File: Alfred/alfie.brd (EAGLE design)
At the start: 83.9 x 45 mm, 33 parts, among them IC1 7805TV, K1 G6A-234P, K2 G6A-234P

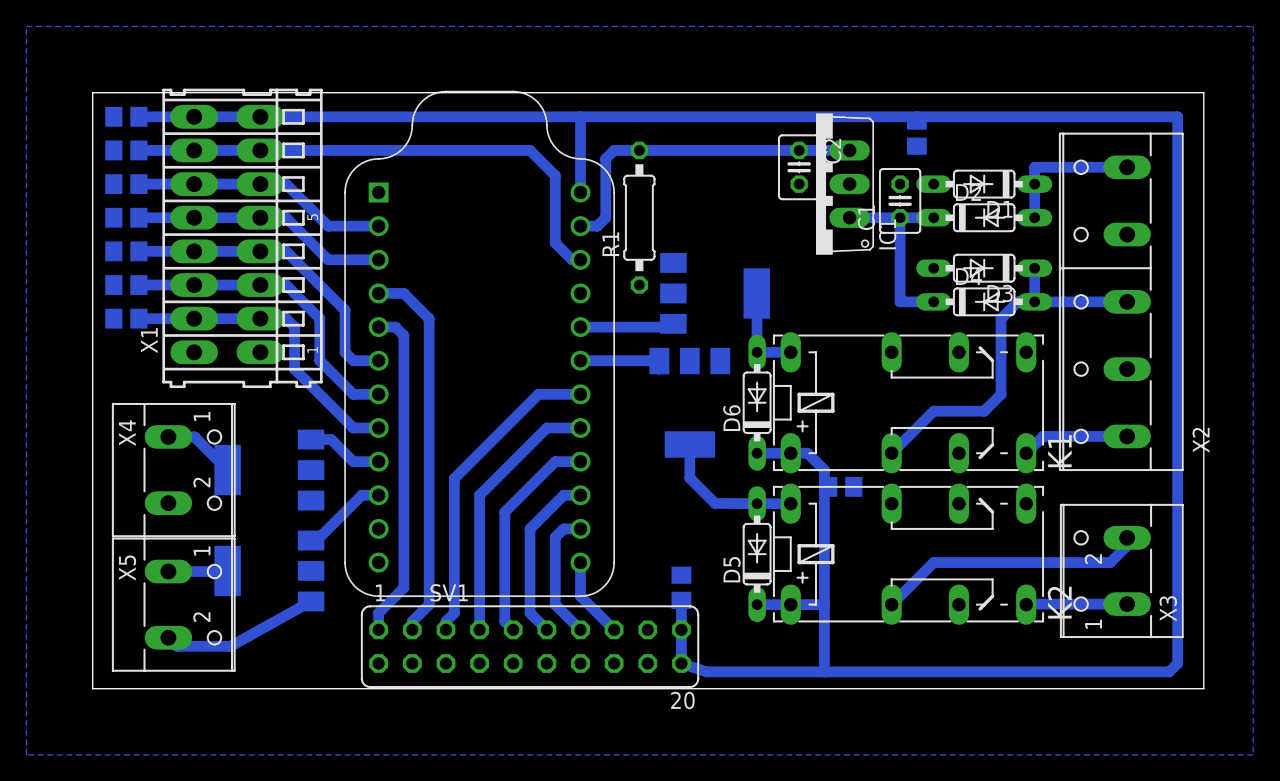
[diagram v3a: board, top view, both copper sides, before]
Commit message: Added bigass cap for relays
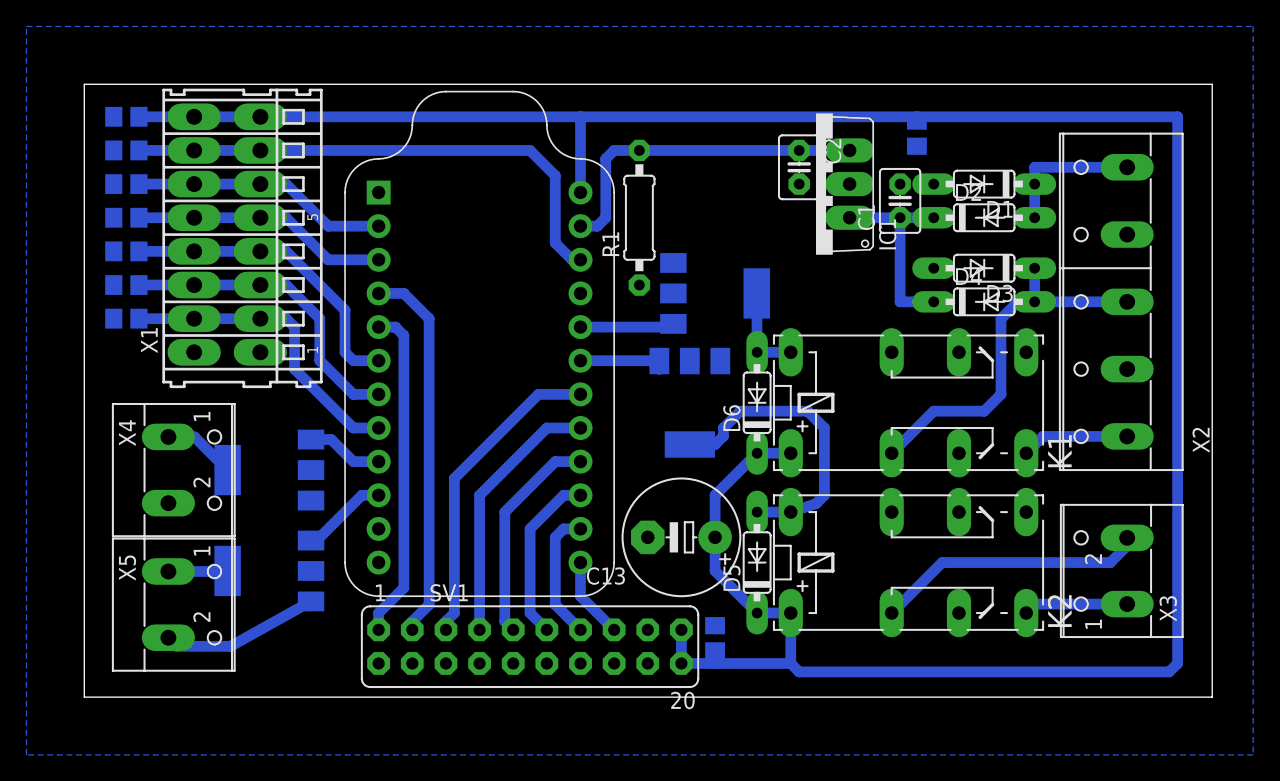
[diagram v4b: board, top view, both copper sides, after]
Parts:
- removed C12: 100nF, rcl:C0805
- added C13: (no value), rcl:E5-8,5
- moved C11 4.58 mm to (47.0, 3.81)
- moved D5 0.63 mm to (50.2, 9.53)
- moved K2 0.63 mm to (56.5, 9.53)
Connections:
- net +5V: now also C13.+; no longer C12.1
- net GND: now also C13.-; no longer C12.2
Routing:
- net N$2: track 10.9 -> 22.6 mm
- net +5V: track 194.6 -> 190.8 mm
- net N$4: track 7.64 -> 8.26 mm
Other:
- board size 83.9 x 45 mm -> 85.2 x 46.3 mm
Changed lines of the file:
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@@
 <board>
 <plain>
-<wire x1="0" y1="0" x2="83.89" y2="0" width="0" layer="20"/>
-<wire x1="83.89" y1="0" x2="83.89" y2="45" width="0" layer="20"/>
-<wire x1="83.89" y1="45" x2="0" y2="45" width="0" layer="20"/>
-<wire x1="0" y1="45" x2="0" y2="0" width="0" layer="20"/>
+<wire x1="-0.635" y1="-0.635" x2="84.525" y2="-0.635" width="0" layer="20"/>
+<wire x1="84.525" y1="-0.635" x2="84.525" y2="45.635" width="0" layer="20"/>
+<wire x1="84.525" y1="45.635" x2="-0.635" y2="45.635" width="0" layer="20"/>
+<wire x1="-0.635" y1="45.635" x2="-0.635" y2="-0.635" width="0" layer="20"/>
 </plain>
 <attributes>
@@
 <param name="rvMicroViaOuter" value="0.25"/>
 <param name="rvMicroViaInner" value="0.25"/>
-<param name="rlMinPadTop" value="10mil"/>
+<param name="rlMinPadTop" value="16mil"/>
 <param name="rlMaxPadTop" value="20mil"/>
-<param name="rlMinPadInner" value="10mil"/>
+<param name="rlMinPadInner" value="16mil"/>
 <param name="rlMaxPadInner" value="20mil"/>
-<param name="rlMinPadBottom" value="10mil"/>
+<param name="rlMinPadBottom" value="16mil"/>
 <param name="rlMaxPadBottom" value="20mil"/>
 <param name="rlMinViaOuter" value="8mil"/>
@@
 <param name="rlMinMicroViaInner" value="4mil"/>
 <param name="rlMaxMicroViaInner" value="20mil"/>
-<param name="psTop" value="-1"/>
-<param name="psBottom" value="-1"/>
+<param name="psTop" value="2"/>
+<param name="psBottom" value="2"/>
 <param name="psFirst" value="-1"/>
 <param name="psElongationLong" value="100"/>
@@
 <param name="checkFont" value="1"/>
 <param name="checkRestrict" value="1"/>
-<param name="useDiameter" value="13"/>
+<param name="useDiameter" value="15"/>
 <param name="maxErrors" value="999999"/>
 </designrules>
@@
 </element>
 <element name="U$5" library="NTF3055L108" package="SOT223" value="NTF3055L108T1GTAB" x="45.085" y="21.59" rot="MR180"/>
-<element name="K2" library="relay" package="G6A-234P" value="G6A-234P" x="56.515" y="10.16">
-<attribute name="OC_NEWARK" value="unknown" x="47.625" y="10.16" size="1.778" layer="27" display="off"/>
-<attribute name="MPN" value="" x="47.625" y="10.16" size="1.778" layer="27" display="off"/>
-<attribute name="MF" value="" x="47.625" y="10.16" size="1.778" layer="27" display="off"/>
-<attribute name="OC_FARNELL" value="unknown" x="47.625" y="10.16" size="1.778" layer="27" display="off"/>
+<element name="K2" library="relay" package="G6A-234P" value="G6A-234P" x="56.515" y="9.525">
+<attribute name="OC_NEWARK" value="unknown" x="47.625" y="9.525" size="1.778" layer="27" display="off"/>
+<attribute name="MPN" value="" x="47.625" y="9.525" size="1.778" layer="27" display="off"/>
+<attribute name="MF" value="" x="47.625" y="9.525" size="1.778" layer="27" display="off"/>
+<attribute name="OC_FARNELL" value="unknown" x="47.625" y="9.525" size="1.778" layer="27" display="off"/>
 </element>
 <element name="X3" library="con-wago-500" package="W237-102" value="" x="76.835" y="8.89" rot="R90">
@@
 <attribute name="OC_FARNELL" value="unknown" x="76.835" y="8.89" size="1.778" layer="27" rot="R90" display="off"/>
 </element>
-<element name="D5" library="diode" package="DO35-7" value="1N4148DO35-7" x="50.165" y="10.16" rot="R90"/>
+<element name="D5" library="diode" package="DO35-7" value="1N4148DO35-7" x="50.165" y="9.525" rot="R90"/>
 <element name="D6" library="diode" package="DO35-7" value="1N4148DO35-7" x="50.165" y="21.59" rot="R90"/>
 <element name="R1" library="rcl" package="0207/10" value="" x="41.275" y="35.56" rot="R90"/>
@@
 <element name="C9" library="rcl" package="C0805" value="100nF" x="2.54" y="43.18" rot="MR0"/>
 <element name="C10" library="rcl" package="C0805" value="100nF" x="62.23" y="41.91" rot="MR270"/>
-<element name="C11" library="rcl" package="C0805" value="100nF" x="44.45" y="7.62" rot="MR90"/>
-<element name="C12" library="rcl" package="C0805" value="100nF" x="56.515" y="15.24" rot="MR180"/>
+<element name="C11" library="rcl" package="C0805" value="100nF" x="46.99" y="3.81" rot="MR90"/>
+<element name="C13" library="rcl" package="E5-8,5" value="" x="44.45" y="11.43" rot="R180"/>
 </elements>
 <signals>
@@
 <wire x1="36.83" y1="37.465" x2="36.83" y2="43.18" width="0.8128" layer="16"/>
 <wire x1="81.915" y1="1.905" x2="81.28" y2="1.27" width="0.8128" layer="16"/>
-<wire x1="81.28" y1="1.27" x2="55.245" y2="1.27" width="0.8128" layer="16"/>
+<wire x1="81.28" y1="1.27" x2="53.34" y2="1.27" width="0.8128" layer="16"/>
 <contactref element="K2" pad="1"/>
-<wire x1="55.245" y1="1.27" x2="46.355" y2="1.27" width="0.8128" layer="16"/>
-<wire x1="55.245" y1="1.27" x2="55.245" y2="6.35" width="0.8128" layer="16"/>
-<wire x1="55.245" y1="6.35" x2="55.245" y2="15.24" width="0.8128" layer="16"/>
-<wire x1="55.245" y1="15.24" x2="55.245" y2="16.51" width="0.8128" layer="16"/>
-<wire x1="55.245" y1="16.51" x2="53.975" y2="17.78" width="0.8128" layer="16"/>
-<wire x1="53.975" y1="17.78" x2="52.705" y2="17.78" width="0.8128" layer="16"/>
-<wire x1="52.705" y1="6.35" x2="55.245" y2="6.35" width="0.8128" layer="16"/>
 <contactref element="D5" pad="C"/>
 <contactref element="D6" pad="C"/>
-<wire x1="50.165" y1="6.35" x2="52.705" y2="6.35" width="0.8128" layer="16"/>
-<wire x1="50.165" y1="17.78" x2="52.705" y2="17.78" width="0.8128" layer="16"/>
 <contactref element="SV1" pad="19"/>
 <contactref element="SV1" pad="20"/>
 <wire x1="44.45" y1="4.445" x2="44.45" y2="1.905" width="0.8128" layer="16"/>
-<wire x1="44.45" y1="1.905" x2="46.355" y2="1.27" width="0.8128" layer="16"/>
 <wire x1="12.66" y1="43.18" x2="36.83" y2="43.18" width="0.8128" layer="16"/>
 <contactref element="C9" pad="1"/>
 <wire x1="12.66" y1="43.18" x2="3.49" y2="43.18" width="0.8128" layer="16"/>
-<contactref element="C12" pad="1"/>
 <contactref element="C11" pad="1"/>
 <contactref element="C10" pad="1"/>
-<wire x1="44.45" y1="6.67" x2="44.45" y2="4.445" width="0.8128" layer="16"/>
-<wire x1="55.565" y1="15.24" x2="55.245" y2="15.24" width="0.8128" layer="16"/>
 <wire x1="62.23" y1="42.86" x2="62.23" y2="43.18" width="0.8128" layer="16"/>
+<contactref element="C13" pad="+"/>
+<wire x1="52.705" y1="17.78" x2="50.165" y2="17.78" width="0.8128" layer="16"/>
+<wire x1="53.34" y1="1.27" x2="52.705" y2="1.905" width="0.8128" layer="16"/>
+<wire x1="52.705" y1="1.905" x2="52.705" y2="5.715" width="0.8128" layer="16"/>
+<wire x1="52.705" y1="5.715" x2="50.165" y2="5.715" width="0.8128" layer="16"/>
+<wire x1="50.165" y1="5.715" x2="46.99" y2="8.89" width="0.8128" layer="16"/>
+<wire x1="46.99" y1="8.89" x2="46.99" y2="11.43" width="0.8128" layer="16"/>
+<wire x1="44.45" y1="1.905" x2="46.99" y2="1.905" width="0.8128" layer="16"/>
+<wire x1="46.99" y1="1.905" x2="52.705" y2="1.905" width="0.8128" layer="16"/>
+<wire x1="46.99" y1="2.86" x2="46.99" y2="1.905" width="0.8128" layer="16"/>
+<wire x1="50.165" y1="17.78" x2="46.99" y2="14.605" width="0.8128" layer="16"/>
+<wire x1="46.99" y1="14.605" x2="46.99" y2="11.43" width="0.8128" layer="16"/>
 </signal>
 <signal name="GND">
@@
 <contactref element="C10" pad="2"/>
 <contactref element="C11" pad="2"/>
-<contactref element="C12" pad="2"/>
+<contactref element="C13" pad="-"/>
 </signal>
 <signal name="DATA0">
@@
 <contactref element="U$5" pad="4"/>
 <contactref element="D5" pad="A"/>
-<wire x1="50.165" y1="13.97" x2="52.705" y2="13.97" width="0.8128" layer="16"/>
-<wire x1="50.165" y1="13.97" x2="46.99" y2="13.995" width="0.8128" layer="16"/>
-<wire x1="46.99" y1="13.995" x2="45.085" y2="15.9" width="0.8128" layer="16"/>
-<wire x1="45.085" y1="15.9" x2="45.085" y2="18.44" width="0.8128" layer="16"/>
+<wire x1="52.705" y1="13.335" x2="50.165" y2="13.335" width="0.8128" layer="16"/>
+<wire x1="45.085" y1="18.44" x2="46.99" y2="18.44" width="0.8128" layer="16"/>
+<wire x1="46.99" y1="18.44" x2="47.625" y2="19.075" width="0.8128" layer="16"/>
+<wire x1="47.625" y1="19.075" x2="47.625" y2="19.685" width="0.8128" layer="16"/>
+<wire x1="47.625" y1="19.685" x2="48.895" y2="20.955" width="0.8128" layer="16"/>
+<wire x1="48.895" y1="20.955" x2="53.975" y2="20.955" width="0.8128" layer="16"/>
+<wire x1="53.975" y1="20.955" x2="55.245" y2="19.685" width="0.8128" layer="16"/>
+<wire x1="55.245" y1="19.685" x2="55.245" y2="14.605" width="0.8128" layer="16"/>
+<wire x1="55.245" y1="14.605" x2="54.61" y2="13.97" width="0.8128" layer="16"/>
+<wire x1="54.61" y1="13.97" x2="52.705" y2="13.335" width="0.8128" layer="16"/>
 </signal>
 <signal name="INNER_DOOR_UNLOCK">
@@
 <contactref element="K2" pad="S1"/>
 <contactref element="X3" pad="1"/>
-<wire x1="70.485" y1="6.35" x2="70.525" y2="6.39" width="0.8128" layer="16"/>
+<wire x1="70.485" y1="5.715" x2="70.525" y2="6.39" width="0.8128" layer="16"/>
 <wire x1="70.525" y1="6.39" x2="78.105" y2="6.39" width="0.8128" layer="16"/>
 </signal>
@@
 <contactref element="K2" pad="P1"/>
 <contactref element="X3" pad="2"/>
-<wire x1="60.325" y1="6.35" x2="63.5" y2="9.525" width="0.8128" layer="16"/>
-<wire x1="63.5" y1="9.525" x2="76.835" y2="9.525" width="0.8128" layer="16"/>
+<wire x1="60.325" y1="5.715" x2="64.135" y2="9.525" width="0.8128" layer="16"/>
+<wire x1="64.135" y1="9.525" x2="76.835" y2="9.525" width="0.8128" layer="16"/>
 <wire x1="76.835" y1="9.525" x2="78.065" y2="10.755" width="0.8128" layer="16"/>
 <wire x1="78.065" y1="10.755" x2="78.105" y2="11.39" width="0.8128" layer="16"/>
@@
 </signal>
 </signals>
+<errors>
+</errors>
 </board>
 </drawing>
